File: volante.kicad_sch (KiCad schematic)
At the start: 1 part, among them U1 AP3012

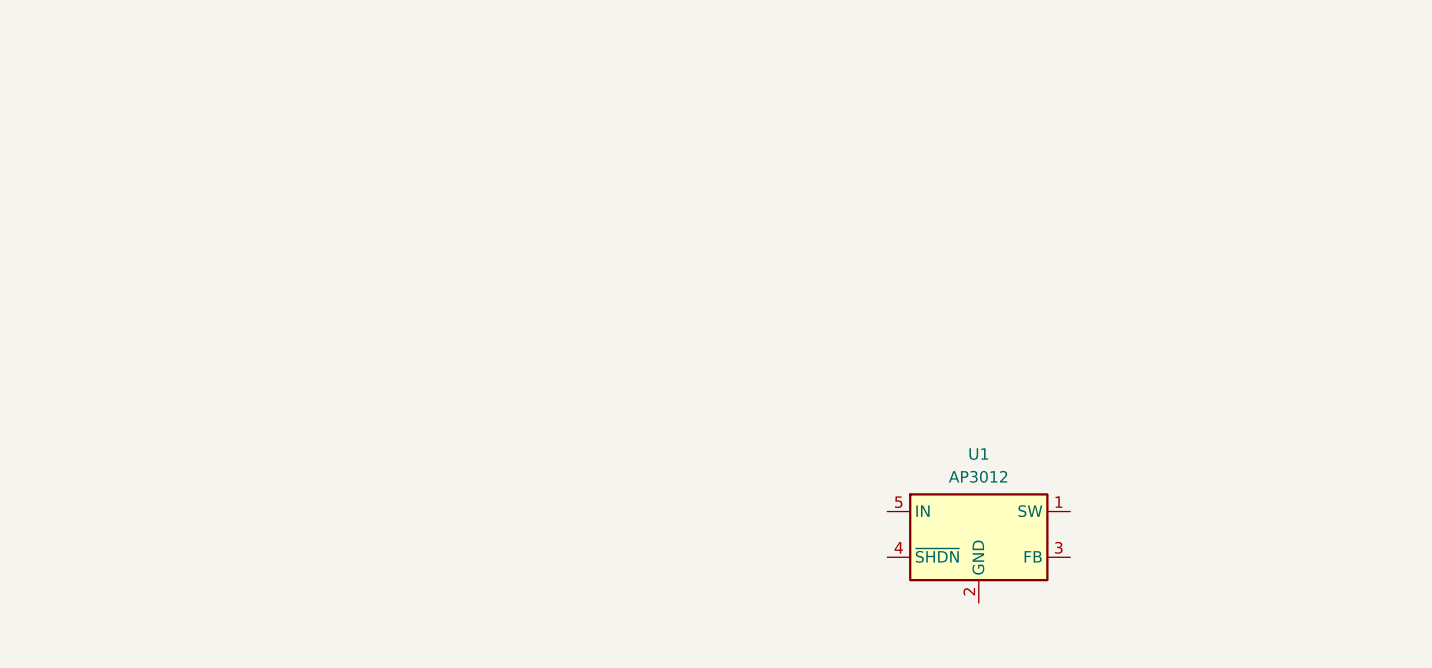
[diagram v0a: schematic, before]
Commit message: Criação das folhas: dc_converter_sch.kicad_sch new file:   h_bridge_sch.kicad_sch
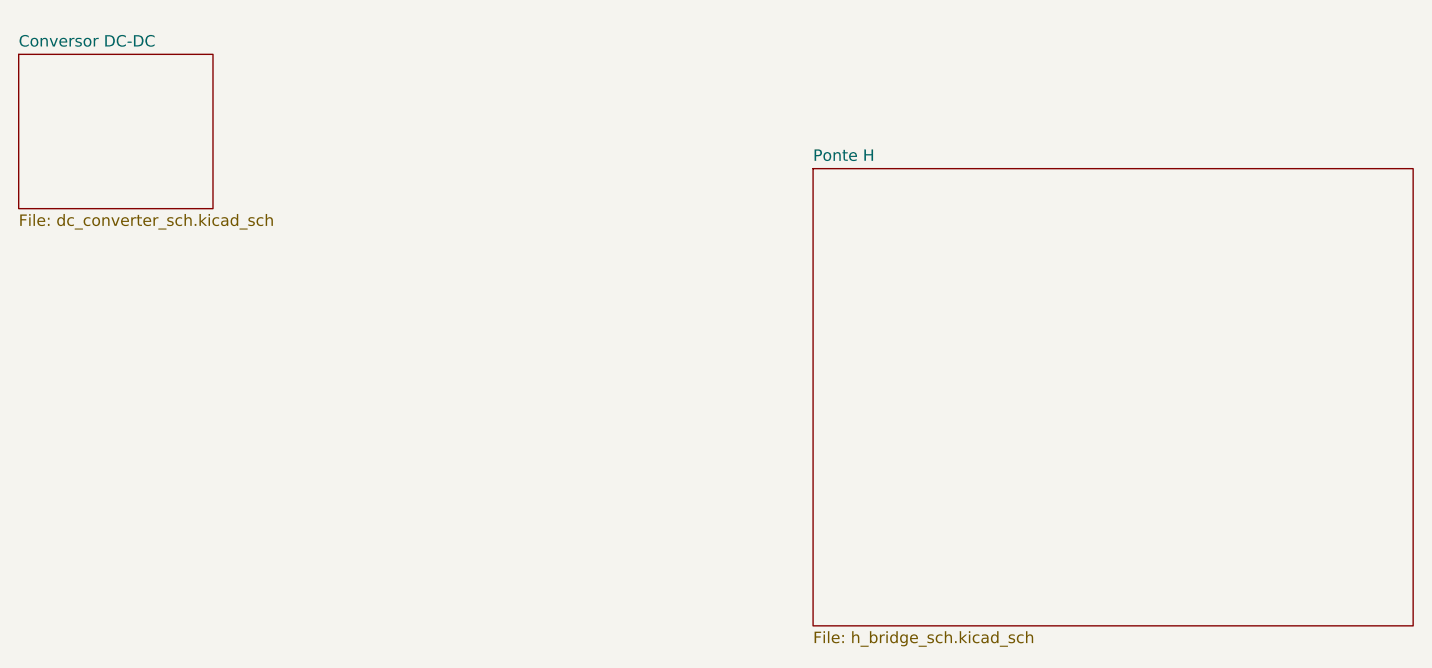
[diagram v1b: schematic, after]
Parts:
- removed U1: AP3012, Package_TO_SOT_SMD:SOT-23-5, symbol Regulator_Switching:AP3012
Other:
- added sheet Conversor DC-DC (dc_converter_sch.kicad_sch)
- added sheet Ponte H (h_bridge_sch.kicad_sch)
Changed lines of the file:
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@@
 	(generator_version "9.0")
 	(paper "A4")
-	(symbol
-		(lib_id "Regulator_Switching:AP3012")
-		(at 127 76.2 0)
-		(unit 1)
+	(sheet
+		(at 20.32 22.86)
+		(size 21.59 17.145)
 		(exclude_from_sim no)
 		(in_bom yes)
@@
 		(dnp no)
 		(fields_autoplaced yes)
-		(property "Reference" "U1"
-			(at 127 67.31 0)
+		(stroke
+			(width 0.1524)
+			(type solid)
+		)
+		(fill
+			(color 0 0 0 0.0000)
+		)
+		(property "Sheetname" "Conversor DC-DC"
+			(at 20.32 22.1484 0)
 			(effects
 				(font
 					(size 1.27 1.27)
 				)
+				(justify left bottom)
 			)
 		)
-		(property "Value" "AP3012"
-			(at 127 69.85 0)
+		(property "Sheetfile" "dc_converter_sch.kicad_sch"
+			(at 20.32 40.5896 0)
 			(effects
 				(font
 					(size 1.27 1.27)
 				)
+				(justify left top)
 			)
 		)
-		(property "Footprint" "Package_TO_SOT_SMD:SOT-23-5"
-			(at 127.635 82.55 0)
-			(effects
-				(font
-					(size 1.27 1.27)
-					(italic yes)
+		(instances
+			(project "volante"
+				(path "/55331ded-e132-41ef-938e-601947036493"
+					(page "2")
 				)
-				(justify left)
-				(hide yes)
 			)
 		)
-		(property "Datasheet" "https://www.diodes.com/assets/Datasheets/AP3012.pdf"
-			(at 127 76.2 0)
+	)
+	(sheet
+		(at 108.585 35.56)
+		(size 66.675 50.8)
+		(exclude_from_sim no)
+		(in_bom yes)
+		(on_board yes)
+		(dnp no)
+		(fields_autoplaced yes)
+		(stroke
+			(width 0.1524)
+			(type solid)
+		)
+		(fill
+			(color 0 0 0 0.0000)
+		)
+		(property "Sheetname" "Ponte H"
+			(at 108.585 34.8484 0)
 			(effects
 				(font
 					(size 1.27 1.27)
 				)
-				(hide yes)
+				(justify left bottom)
 			)
 		)
-		(property "Description" "500mA, Adjustable Step-Up Voltage Regulator, 1.5MHz Frequency, SOT-23-5"
-			(at 127 76.2 0)
+		(property "Sheetfile" "h_bridge_sch.kicad_sch"
+			(at 108.585 86.9446 0)
 			(effects
 				(font
 					(size 1.27 1.27)
 				)
-				(hide yes)
+				(justify left top)
 			)
 		)
-		(pin "1"
-		)
-		(pin "2"
-		)
-		(pin "5"
-		)
-		(pin "4"
-		)
-		(pin "3"
-		)
 		(instances
-			(project ""
+			(project "volante"
 				(path "/55331ded-e132-41ef-938e-601947036493"
-					(reference "U1")
-					(unit 1)
+					(page "3")
 				)
 			)

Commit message: alteração no circuito de ponte h e inicio da criação da PCB
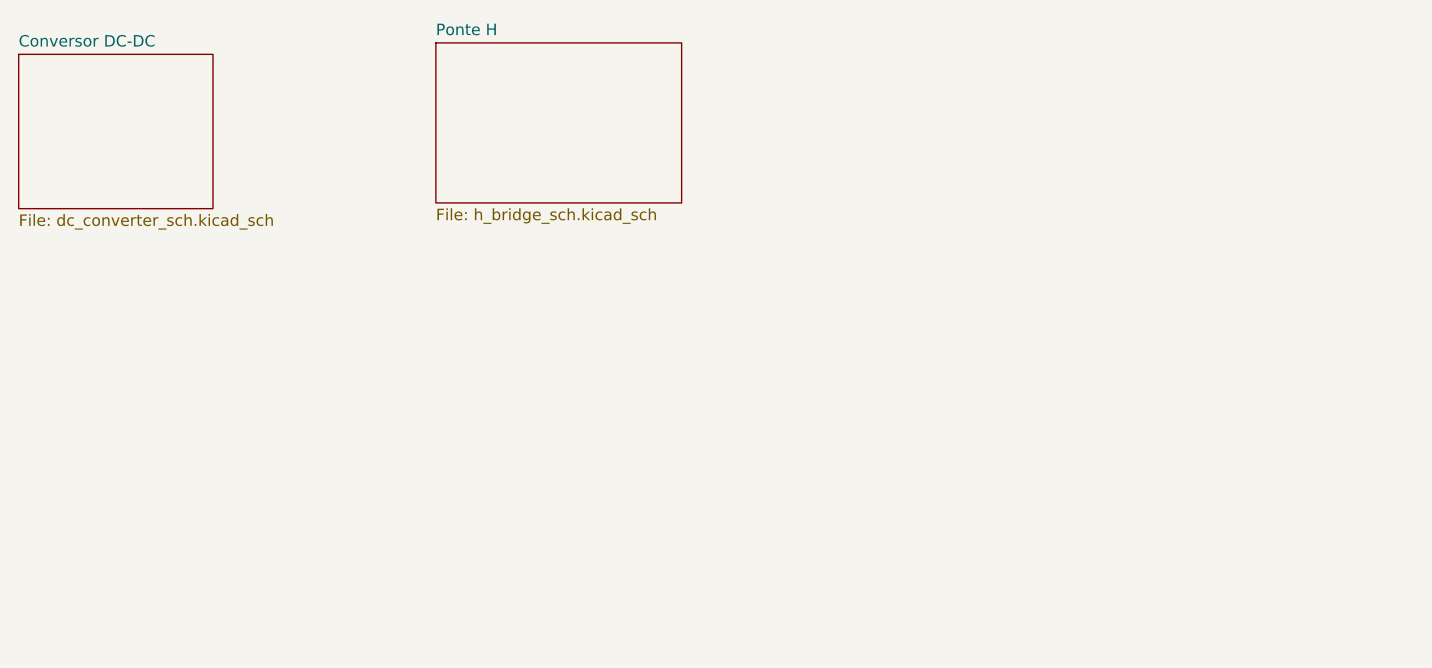
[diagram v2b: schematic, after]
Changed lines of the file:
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@@
 	)
 	(sheet
-		(at 108.585 35.56)
-		(size 66.675 50.8)
+		(at 66.675 21.59)
+		(size 27.305 17.78)
 		(exclude_from_sim no)
 		(in_bom yes)
@@
 		)
 		(property "Sheetname" "Ponte H"
-			(at 108.585 34.8484 0)
+			(at 66.675 20.8784 0)
 			(effects
 				(font
@@
 		)
 		(property "Sheetfile" "h_bridge_sch.kicad_sch"
-			(at 108.585 86.9446 0)
+			(at 66.675 39.9546 0)
 			(effects
 				(font

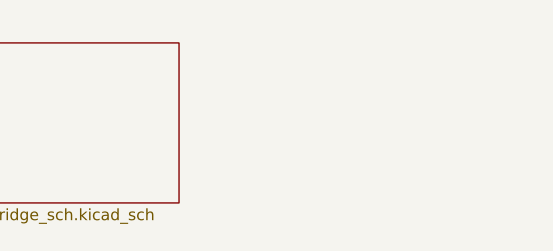
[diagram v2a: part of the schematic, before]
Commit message: foi adicionado o arduino e conector de encoder na mesma placa, utilizando optacopladores recomeço do layout pcb
 Changes to be committed:
	new file:   controle.kicad_sch
	modified:   dc_converter_sch.kicad_sch
	modified:   half_bridge.kicad_sch
	modified:   volante.kicad_pcb
	modified:   volante.kicad_prl
	modified:   volante.kicad_pro
	modified:   volante.kicad_sch
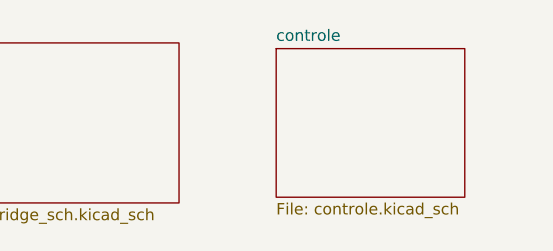
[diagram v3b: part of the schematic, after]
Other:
- added sheet controle (controle.kicad_sch)
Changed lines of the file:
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@@
 	(paper "A4")
+	(sheet
+		(at 104.775 22.225)
+		(size 20.955 16.51)
+		(exclude_from_sim no)
+		(in_bom yes)
+		(on_board yes)
+		(dnp no)
+		(fields_autoplaced yes)
+		(stroke
+			(width 0.1524)
+			(type solid)
+		)
+		(fill
+			(color 0 0 0 0.0000)
+		)
+		(property "Sheetname" "controle"
+			(at 104.775 21.5134 0)
+			(effects
+				(font
+					(size 1.27 1.27)
+				)
+				(justify left bottom)
+			)
+		)
+		(property "Sheetfile" "controle.kicad_sch"
+			(at 104.775 39.3196 0)
+			(effects
+				(font
+					(size 1.27 1.27)
+				)
+				(justify left top)
+			)
+		)
+		(instances
+			(project "volante"
+				(path "/55331ded-e132-41ef-938e-601947036493"
+					(page "6")
+				)
+			)
+		)
+	)
 	(sheet
 		(at 20.32 22.86)
